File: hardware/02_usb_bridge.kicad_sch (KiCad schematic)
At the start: 73 parts, among them J201 X6511WVS-08H-C60D48R1, J202 X6511WVS-05H-C60D48R1, Q207 AO3400A, U201 CH32V307RCT6, U202 AGRV2KQ32, U205 74LVC1G157, U206 74LVC1G11, U208 74LVC3G34, X201 80.000 MHz, X202 49.152 MHz, X203 45.1584 MHz, Y201 8 MHz

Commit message: feat: close the last link by hand (ECO F09 CPLD_IRQ to pin 3); 0 ratsnest links, 0 DRC
- ECO F09: CPLD_IRQ moves from U202 pin 29 (sealed under LINK_MISO's escape
  via) to west-row I/O pin 3; schematic overlay, approved delta and
  02_usb_bridge sheet regenerated; RTL pin constraint must follow.
- Hand routes: U201.39 escape to a 0.5 mm via; 3V3D via-to-via link moved
  from B.Cu to L3; CPLD_IRQ B.Cu/L4/L3 path to pin 3; CPLD_NRST pin-4 stub
  re-routed; LINK_MISO via nudged clear of NC pin 29.
- Result: 0 unconnected, 0 DRC errors/warnings, 544 footprints placed,
  VALIDATE_OK, schematic verification and ERC pass. EMS layout audit refreshed.

Co-Authored-By: Claude Opus 5.5 <noreply@anthropic.com>
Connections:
- net CPLD_IRQ: now also U202.3 (IO/PIN_3); no longer U202.29 (IO/PIN_29)
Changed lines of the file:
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@@
 (global_label "FAM_CLK" (shape bidirectional) (at 118.11 63.5 180) (effects (font (size 0.762 0.762)) (justify right bottom)))
 (no_connect (at 120.65 66.04))
-(no_connect (at 120.65 68.58))
+(wire (pts (xy 120.65 68.58) (xy 118.11 68.58)) (stroke (width 0) (type solid)))
+(global_label "CPLD_IRQ" (shape bidirectional) (at 118.11 68.58 180) (effects (font (size 0.762 0.762)) (justify right bottom)))
 (wire (pts (xy 120.65 71.12) (xy 118.11 71.12)) (stroke (width 0) (type solid)))
 (global_label "CPLD_NRST" (shape bidirectional) (at 118.11 71.12 180) (effects (font (size 0.762 0.762)) (justify right bottom)))
@@
 (wire (pts (xy 171.45 88.9) (xy 173.99 88.9)) (stroke (width 0) (type solid)))
 (global_label "LINK_MISO" (shape bidirectional) (at 173.99 88.9 0) (effects (font (size 0.762 0.762)) (justify left bottom)))
-(wire (pts (xy 171.45 91.44) (xy 173.99 91.44)) (stroke (width 0) (type solid)))
-(global_label "CPLD_IRQ" (shape bidirectional) (at 173.99 91.44 0) (effects (font (size 0.762 0.762)) (justify left bottom)))
+(no_connect (at 171.45 91.44))
 (wire (pts (xy 171.45 93.98) (xy 173.99 93.98)) (stroke (width 0) (type solid)))
 (global_label "GND" (shape bidirectional) (at 173.99 93.98 0) (effects (font (size 0.762 0.762)) (justify left bottom)))

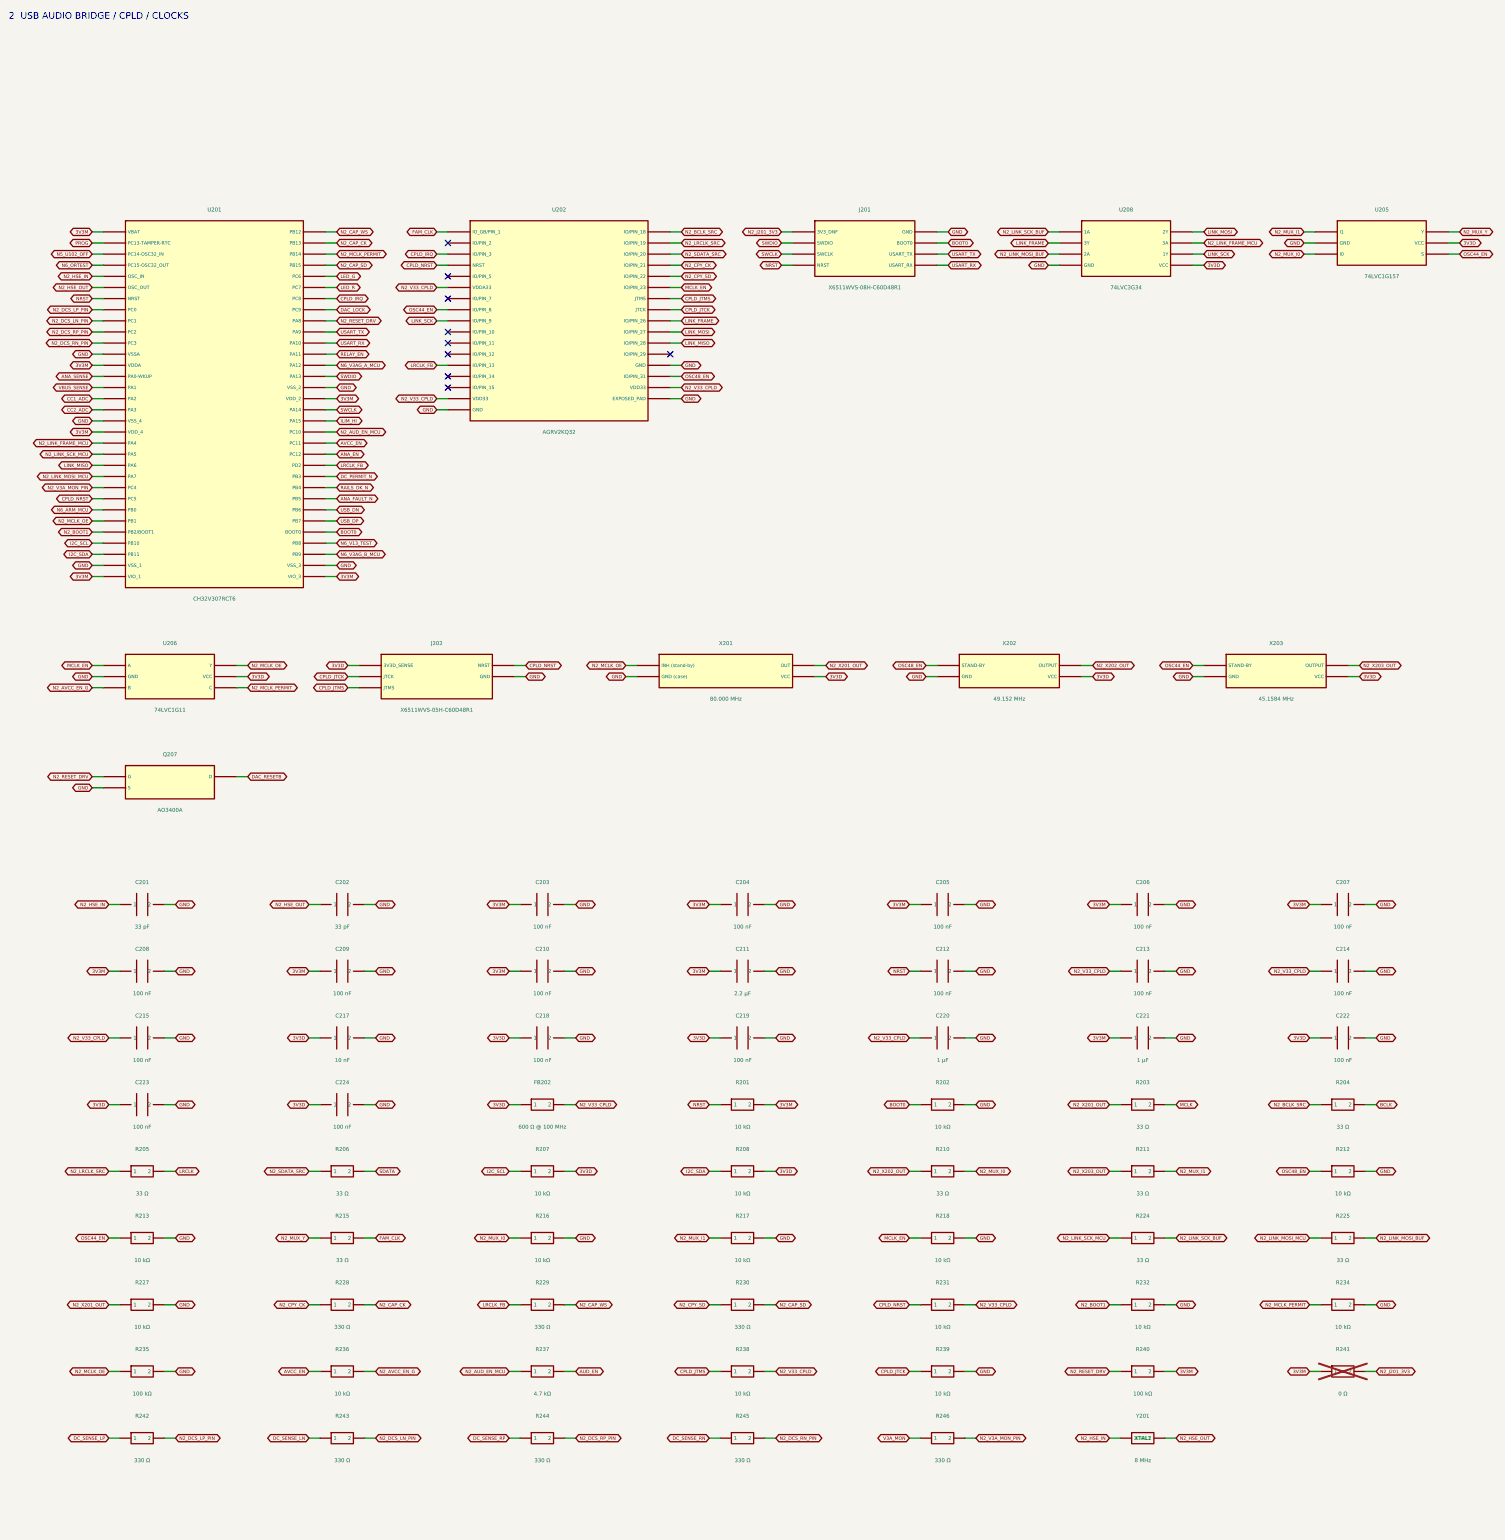
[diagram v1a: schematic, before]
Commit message: fix: close the independent layout review v1.0 (T1-T7, D1-D3); verified on the reviewer's solvers
Layout (blocks b25-b33, replayed by the generator):
- T1 MCLK-alive detector: C625/R666/R667 in a row at D609; hold node 3.4 mm, no vias (was 68 mm,
  8 vias). The old trunk becomes the DC side N6_MCK_CMP. TP747 behind R667 (ECO F13).
- T2 ECO F11: R247-R249, 33 ohm, at the U208 LINK outputs; R249 returns on In3; C224 above U208.
- T3 ECO F12: R203 33 ohm -> 0 ohm (BOM only).
- T4 six filled 0.7/0.3 vias in the U503 PowerPAD; 3V3M/ANA_EN/AUD_EN/N5_ILIM detours.
- T5 C217/C218/C219 at the X201-X203 VCC pins (X203 shifted 1 mm, R218 relocated).
- T6 C206/C207 to U201 pins 64/32 (pins 1/19: no legal site).
- EP vias U504 +2, U401 +3, U402 +4; J701 sleeve 2 -> 5 GND vias; R1 board corner fixed.

Generator: schematic sync (fields, DNP, NC-pin nets) gives 0 parity issues (T7, D3); ECO footprint
copies get fresh UUIDs; value overrides. New CI step check_integrated_parity.py (DRC + parity).

Re-verified with the reviewer's evidence code on the new board (sim/layout_review_v1):
detector dead-worst 0.481 -> 0.458 ms; LINK_SCK clamp 14.3 -> 0 mA; U503 fault 131.3 -> 117.9 C;
oscillator spikes 175-189 -> 60-69 mV; MCU droop pins 32/64 102-103 -> 41/30 mV.

Docs: LAYOUT_REVIEW_RESPONSE_2026-10-13.md, DESIGN_DOCUMENT_UPDATES_2026-10-13.md (Parts List
v1.0 and Spec/Notes change lists for the owner), DESIGN_TO_LAYOUT_DIFFERENCES.md, 1:1 print for T8.

Co-Authored-By: Claude Opus 5.5 <noreply@anthropic.com>
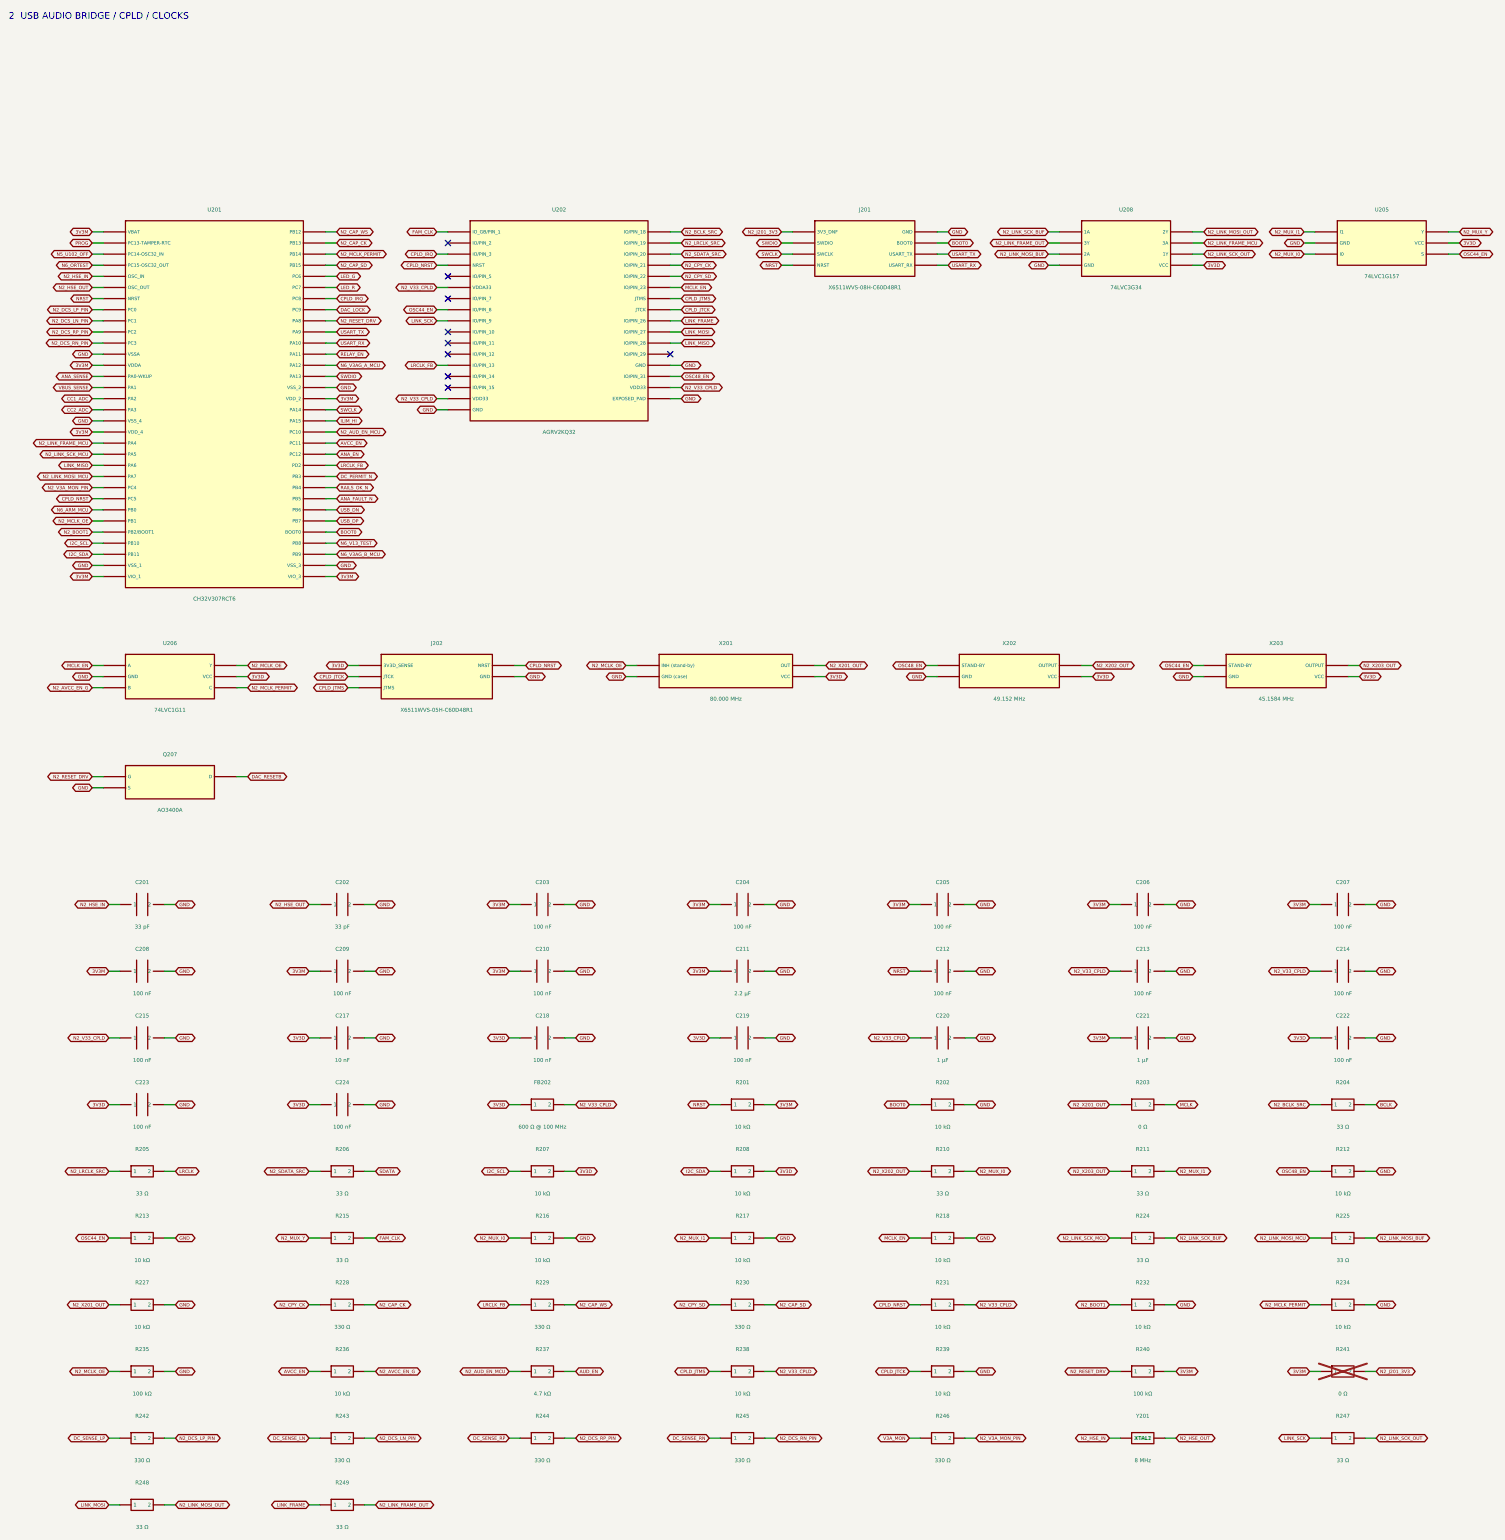
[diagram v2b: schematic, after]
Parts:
- added R247, R248, R249: 33 Ω, Resistor_SMD:R_0402_1005Metric, symbol DAC_HPA:P9007
- R203: value 33 Ω -> 0 Ω; symbol DAC_HPA:P030 -> DAC_HPA:P9008; LCSC C25105 -> C17168; LCSC Part # C25105 -> C17168; MPN UNI-ROYAL 0402WGF330JTCE -> UNI-ROYAL 0402WGF0000TCE; Rating/Tolerance 1 %, 62.5 mW -> jumper; Workbook Value 33 Ω -> — (functional ECO; absent from Parts List v0.9)
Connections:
- net LINK_FRAME: now also R249.1; no longer U208.2 (3Y)
- net LINK_MOSI: now also R248.1; no longer U208.5 (2Y)
- net LINK_SCK: now also R247.1; no longer U208.7 (1Y)
- new net N2_LINK_FRAME_OUT: R249.2, U208.2 (3Y)
- new net N2_LINK_MOSI_OUT: R248.2, U208.5 (2Y)
- new net N2_LINK_SCK_OUT: R247.2, U208.7 (1Y)

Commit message: feat: LCSC numbers for X202 (C17466132) and X203 (C17523715)
Owner-supplied JLC numbers for the NDK oscillators, listed by JLC under the
spec code (NSC5083D = 3.3 V NZ2520SDA; "45.158M" is 45.1584 MHz truncated).
Every placed BOM line now has an LCSC number. C17523715 and C4101918 are
pre-order parts.

Co-Authored-By: Claude Opus 5.5 <noreply@anthropic.com>
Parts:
- X202: LCSC — -> C17466132; LCSC Part # — -> C17466132; Source Global sourcing -> JLCPCB C17466132 (48 in stock on 19 Oct 2026)
- X203: LCSC — -> C17523715; LCSC Part # — -> C17523715; Source Global sourcing -> JLCPCB C17523715 (pre-order, 0 stock on 19 Oct 2026)
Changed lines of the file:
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@@
 (property "Datasheet" "https://www.ndk.com/en/products/upload/lineup/pdf/NDKT02-00008_en.pdf" (at 248.92 163.83 0) (effects (font (size 1.016 1.016)) (hide yes)))
 (property "MPN" "NDK NZ2520SDA-49.152MHZ-NSC5083D" (at 248.92 163.83 0) (effects (font (size 1.016 1.016)) (hide yes)))
-(property "LCSC" "—" (at 248.92 163.83 0) (effects (font (size 1.016 1.016)) (hide yes)))
-(property "LCSC Part #" "—" (at 248.92 163.83 0) (effects (font (size 1.016 1.016)) (hide yes)))
+(property "LCSC" "C17466132" (at 248.92 163.83 0) (effects (font (size 1.016 1.016)) (hide yes)))
+(property "LCSC Part #" "C17466132" (at 248.92 163.83 0) (effects (font (size 1.016 1.016)) (hide yes)))
 (property "Assembly" "Yes" (at 248.92 163.83 0) (effects (font (size 1.016 1.016)) (hide yes)))
 (property "Package" "2.5 × 2.0 mm 4-pad, plain 2520 land" (at 248.92 163.83 0) (effects (font (size 1.016 1.016)) (hide yes)))
 (property "Rating/Tolerance" "±50 ppm overall, 15 mA max, 35 µA stand-by" (at 248.92 163.83 0) (effects (font (size 1.016 1.016)) (hide yes)))
-(property "Source" "Global sourcing" (at 248.92 163.83 0) (effects (font (size 1.016 1.016)) (hide yes)))
+(property "Source" "JLCPCB C17466132 (48 in stock on 19 Oct 2026)" (at 248.92 163.83 0) (effects (font (size 1.016 1.016)) (hide yes)))
 (property "Workbook Value" "49.152 MHz" (at 248.92 163.83 0) (effects (font (size 1.016 1.016)) (hide yes)))
 (property "Footprint status" "VERIFY G-3" (at 248.92 163.83 0) (effects (font (size 1.016 1.016)) (hide yes)))
@@
 (property "Datasheet" "https://www.ndk.com/en/products/upload/lineup/pdf/NDKT02-00008_en.pdf" (at 309.88 163.83 0) (effects (font (size 1.016 1.016)) (hide yes)))
 (property "MPN" "NDK NZ2520SDA-45.1584MHZ-NSC5083D" (at 309.88 163.83 0) (effects (font (size 1.016 1.016)) (hide yes)))
-(property "LCSC" "—" (at 309.88 163.83 0) (effects (font (size 1.016 1.016)) (hide yes)))
-(property "LCSC Part #" "—" (at 309.88 163.83 0) (effects (font (size 1.016 1.016)) (hide yes)))
+(property "LCSC" "C17523715" (at 309.88 163.83 0) (effects (font (size 1.016 1.016)) (hide yes)))
+(property "LCSC Part #" "C17523715" (at 309.88 163.83 0) (effects (font (size 1.016 1.016)) (hide yes)))
 (property "Assembly" "Yes" (at 309.88 163.83 0) (effects (font (size 1.016 1.016)) (hide yes)))
 (property "Package" "2.5 × 2.0 mm 4-pad, plain 2520 land" (at 309.88 163.83 0) (effects (font (size 1.016 1.016)) (hide yes)))
 (property "Rating/Tolerance" "±50 ppm overall, 15 mA max, 35 µA stand-by" (at 309.88 163.83 0) (effects (font (size 1.016 1.016)) (hide yes)))
-(property "Source" "Global sourcing" (at 309.88 163.83 0) (effects (font (size 1.016 1.016)) (hide yes)))
+(property "Source" "JLCPCB C17523715 (pre-order, 0 stock on 19 Oct 2026)" (at 309.88 163.83 0) (effects (font (size 1.016 1.016)) (hide yes)))
 (property "Workbook Value" "45.1584 MHz" (at 309.88 163.83 0) (effects (font (size 1.016 1.016)) (hide yes)))
 (property "Footprint status" "VERIFY G-3" (at 309.88 163.83 0) (effects (font (size 1.016 1.016)) (hide yes)))
